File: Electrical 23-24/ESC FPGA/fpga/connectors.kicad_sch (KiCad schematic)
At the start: 2 parts, among them J3 USB_B_Micro

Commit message: Made BOM, need to modify footprints
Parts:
- added J5, J6: Conn_02x06_Top_Bottom, Connector_PinSocket_2.54mm:PinSocket_2x06_P2.54mm_Horizontal, symbol Connector_Generic:Conn_02x06_Top_Bottom
- added J7: Conn_02x20_Odd_Even, Connector_PinSocket_2.54mm:PinSocket_2x20_P2.54mm_Vertical, symbol Connector_Generic:Conn_02x20_Odd_Even
- added J8: Conn_02x06_Top_Bottom, Connector_PinSocket_2.54mm:PinSocket_2x06_P2.54mm_Vertical, symbol Connector_Generic:Conn_02x06_Top_Bottom
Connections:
- net GND: now also J5.11 (Pin_11), J5.5 (Pin_5), J6.11 (Pin_11), J6.5 (Pin_5), J7.14 (Pin_14), J7.20 (Pin_20), J7.25 (Pin_25), J7.30 (Pin_30), J7.34 (Pin_34), J7.39 (Pin_39), J7.6 (Pin_6), J7.9 (Pin_9), J8.12 (Pin_12), J8.6 (Pin_6)
- net VBATT: now also J8.1 (Pin_1), J8.7 (Pin_7)
- net VUSB: now also J7.2 (Pin_2), J7.4 (Pin_4), J8.2 (Pin_2), J8.8 (Pin_8)
- new net 1V2: J8.11 (Pin_11), J8.5 (Pin_5)
- new net 2V5: J8.10 (Pin_10), J8.4 (Pin_4)
- new net 3V3: J5.12 (Pin_12), J5.6 (Pin_6), J6.12 (Pin_12), J6.6 (Pin_6), J7.1 (Pin_1), J7.17 (Pin_17), J8.3 (Pin_3), J8.9 (Pin_9)
- new net GPIO0: J7.27 (Pin_27)
- new net GPIO1: J7.28 (Pin_28)
- new net GPIO10: J7.19 (Pin_19)
- new net GPIO11: J7.23 (Pin_23)
- new net GPIO12: J7.32 (Pin_32)
- new net GPIO13: J7.33 (Pin_33)
- new net GPIO14: J7.8 (Pin_8)
- new net GPIO15: J7.10 (Pin_10)
- new net GPIO16: J7.36 (Pin_36)
- new net GPIO17: J7.11 (Pin_11)
- new net GPIO18: J7.12 (Pin_12)
- new net GPIO19: J7.35 (Pin_35)
- new net GPIO2: J7.3 (Pin_3)
- new net GPIO20: J7.38 (Pin_38)
- new net GPIO21: J7.40 (Pin_40)
- new net GPIO22: J7.15 (Pin_15)
- new net GPIO23: J7.16 (Pin_16)
- new net GPIO24: J7.18 (Pin_18)
- new net GPIO25: J7.22 (Pin_22)
- new net GPIO26: J7.37 (Pin_37)
- new net GPIO27: J7.13 (Pin_13)
- new net GPIO3: J7.5 (Pin_5)
- new net GPIO4: J7.7 (Pin_7)
- new net GPIO5: J7.29 (Pin_29)
- new net GPIO6: J7.31 (Pin_31)
- new net GPIO7: J7.26 (Pin_26)
- new net GPIO8: J7.24 (Pin_24)
- new net GPIO9: J7.21 (Pin_21)
- new net PMOD1_0: J5.1 (Pin_1)
- new net PMOD1_1: J5.2 (Pin_2)
- new net PMOD1_2: J5.3 (Pin_3)
- new net PMOD1_3: J5.4 (Pin_4)
- new net PMOD1_4: J5.7 (Pin_7)
- new net PMOD1_5: J5.8 (Pin_8)
- new net PMOD1_6: J5.9 (Pin_9)
- new net PMOD1_7: J5.10 (Pin_10)
- new net PMOD2_0: J6.1 (Pin_1)
- new net PMOD2_1: J6.2 (Pin_2)
- new net PMOD2_2: J6.3 (Pin_3)
- new net PMOD2_3: J6.4 (Pin_4)
- new net PMOD2_4: J6.7 (Pin_7)
- new net PMOD2_5: J6.8 (Pin_8)
- new net PMOD2_6: J6.9 (Pin_9)
- new net PMOD2_7: J6.10 (Pin_10)
- no-connect marks 4 -> 5

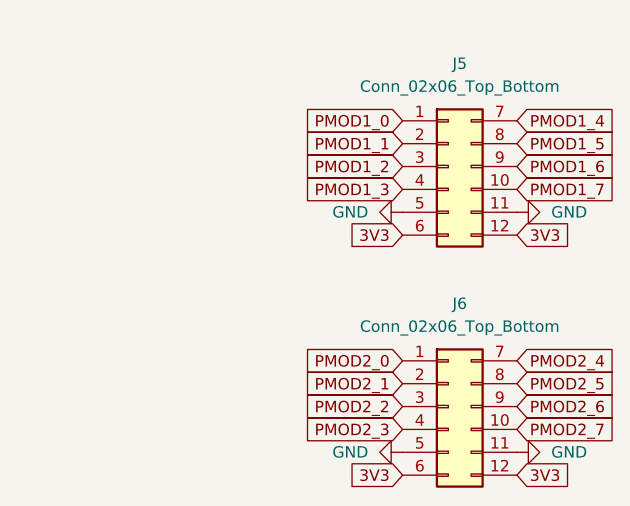
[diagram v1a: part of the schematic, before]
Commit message: Finish groupings on FPGA PCB
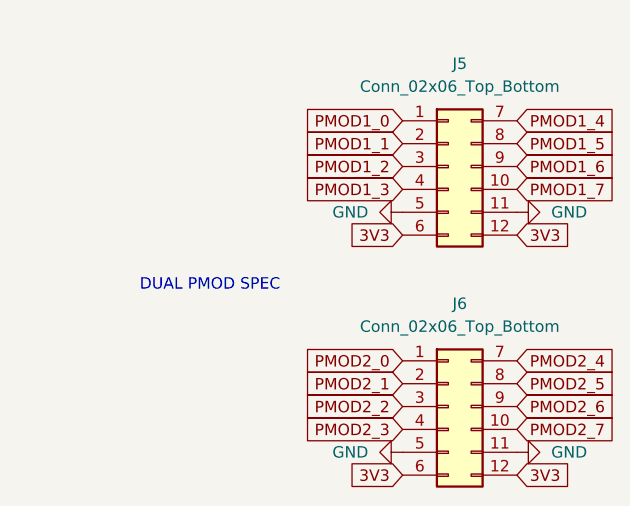
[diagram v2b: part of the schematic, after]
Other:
- note added: "DUAL PMOD SPEC"
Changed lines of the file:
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@@
   (no_connect (at 36.83 35.56))
   (no_connect (at 36.83 33.02))
+  (text "DUAL PMOD SPEC" (at 35.56 105.41 0)
+    (effects (font (size 1.27 1.27)) (justify left bottom))
+  )
   (global_label "PMOD2_1" (shape input) (at 64.77 115.57 180) (fields_autoplaced)
     (effects (font (size 1.27 1.27)) (justify right))

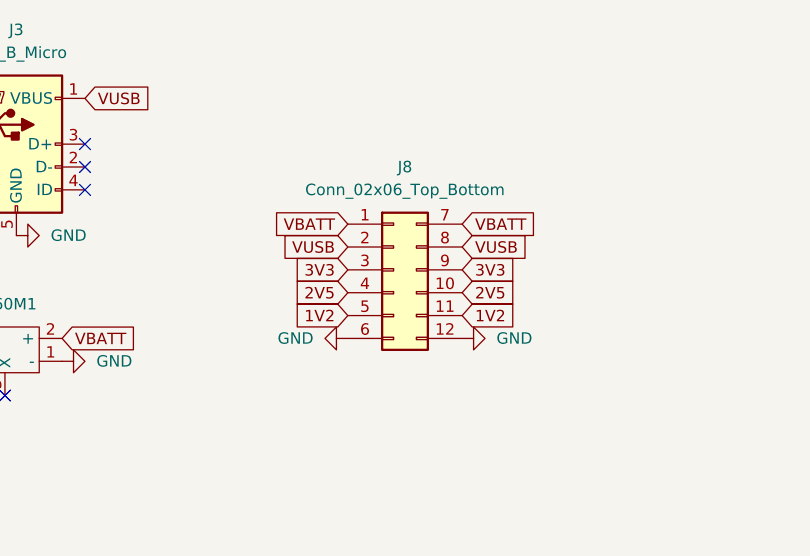
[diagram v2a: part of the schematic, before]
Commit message: Finished hard signal routing, need PMOD and Power
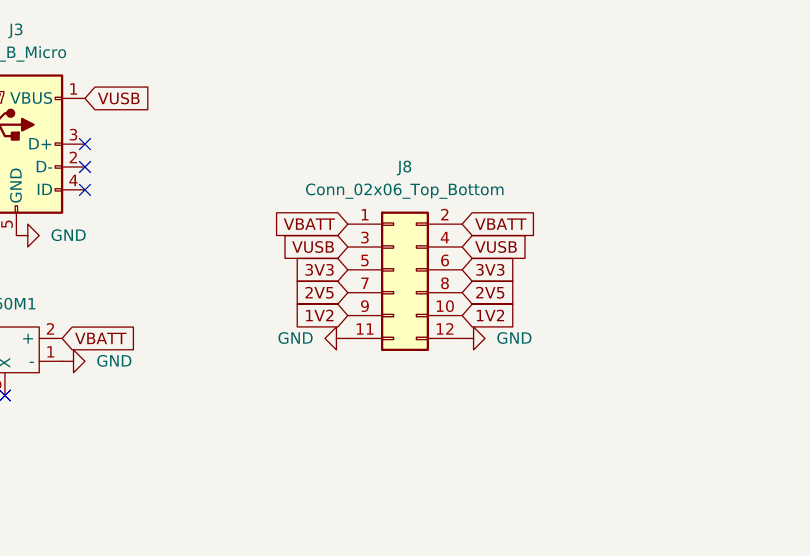
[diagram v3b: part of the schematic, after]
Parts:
- J8: symbol Connector_Generic:Conn_02x06_Top_Bottom -> Connector_Generic:Conn_02x06_Odd_Even
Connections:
- net 1V2: now also J8.10 (Pin_10), J8.9 (Pin_9); no longer J8.11 (Pin_11), J8.5 (Pin_5)
- net 2V5: now also J8.7 (Pin_7), J8.8 (Pin_8); no longer J8.10 (Pin_10), J8.4 (Pin_4)
- net 3V3: now also J8.5 (Pin_5), J8.6 (Pin_6); no longer J8.3 (Pin_3), J8.9 (Pin_9)
- net GND: now also J8.11 (Pin_11); no longer J8.6 (Pin_6)
- net VBATT: now also J8.2 (Pin_2); no longer J8.7 (Pin_7)
- net VUSB: now also J8.3 (Pin_3), J8.4 (Pin_4); no longer J8.2 (Pin_2), J8.8 (Pin_8)
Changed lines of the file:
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@@
     )
   )
-  (symbol (lib_id "Connector_Generic:Conn_02x06_Top_Bottom") (at 71.12 46.99 0) (unit 1)
+  (symbol (lib_id "Connector_Generic:Conn_02x06_Odd_Even") (at 71.12 46.99 0) (unit 1)
     (in_bom yes) (on_board yes) (dnp no) (fields_autoplaced)
     (property "Reference" "J8" (at 72.39 35.56 0)
@@
       (effects (font (size 1.27 1.27)) hide)
     )
-    (property "Datasheet" "https://www.digikey.com/en/products/detail/sullins-connector-solutions/PPTC062LFBN-RC/810212" (at 71.12 46.99 0)
+    (property "Datasheet" "~" (at 71.12 46.99 0)
       (effects (font (size 1.27 1.27)) hide)
     )

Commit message: Finish PCB layout, need to DRC
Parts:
- J5, J6: symbol Connector_Generic:Conn_02x06_Top_Bottom -> Connector_Generic:Conn_02x06_Odd_Even
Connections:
- net 3V3: now also J5.11 (Pin_11), J6.11 (Pin_11); no longer J5.6 (Pin_6), J6.6 (Pin_6)
- net GND: now also J5.10 (Pin_10), J5.9 (Pin_9), J6.10 (Pin_10), J6.9 (Pin_9); no longer J5.11 (Pin_11), J5.5 (Pin_5), J6.11 (Pin_11), J6.5 (Pin_5)
- net PMOD1_1: now also J5.3 (Pin_3); no longer J5.2 (Pin_2)
- net PMOD1_2: now also J5.5 (Pin_5); no longer J5.3 (Pin_3)
- net PMOD1_3: now also J5.7 (Pin_7); no longer J5.4 (Pin_4)
- net PMOD1_4: now also J5.2 (Pin_2); no longer J5.7 (Pin_7)
- net PMOD1_5: now also J5.4 (Pin_4); no longer J5.8 (Pin_8)
- net PMOD1_6: now also J5.6 (Pin_6); no longer J5.9 (Pin_9)
- net PMOD1_7: now also J5.8 (Pin_8); no longer J5.10 (Pin_10)
- net PMOD2_1: now also J6.3 (Pin_3); no longer J6.2 (Pin_2)
- net PMOD2_2: now also J6.5 (Pin_5); no longer J6.3 (Pin_3)
- net PMOD2_3: now also J6.7 (Pin_7); no longer J6.4 (Pin_4)
- net PMOD2_4: now also J6.2 (Pin_2); no longer J6.7 (Pin_7)
- net PMOD2_5: now also J6.4 (Pin_4); no longer J6.8 (Pin_8)
- net PMOD2_6: now also J6.6 (Pin_6); no longer J6.9 (Pin_9)
- net PMOD2_7: now also J6.8 (Pin_8); no longer J6.10 (Pin_10)
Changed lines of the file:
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@@
     )
   )
-  (symbol (lib_id "Connector_Generic:Conn_02x06_Top_Bottom") (at 69.85 118.11 0) (unit 1)
+  (symbol (lib_id "Connector_Generic:Conn_02x06_Odd_Even") (at 69.85 118.11 0) (unit 1)
     (in_bom yes) (on_board yes) (dnp no) (fields_autoplaced)
     (property "Reference" "J6" (at 71.12 106.68 0)
@@
       (effects (font (size 1.27 1.27)) hide)
     )
-    (property "Datasheet" "https://www.digikey.com/en/products/detail/sullins-connector-solutions/PPTC062LJBN-RC/775978" (at 69.85 118.11 0)
+    (property "Datasheet" "~" (at 69.85 118.11 0)
       (effects (font (size 1.27 1.27)) hide)
     )
@@
     )
   )
-  (symbol (lib_id "Connector_Generic:Conn_02x06_Top_Bottom") (at 69.85 91.44 0) (unit 1)
+  (symbol (lib_id "Connector_Generic:Conn_02x06_Odd_Even") (at 69.85 91.44 0) (unit 1)
     (in_bom yes) (on_board yes) (dnp no) (fields_autoplaced)
     (property "Reference" "J5" (at 71.12 80.01 0)
@@
       (effects (font (size 1.27 1.27)) hide)
     )
-    (property "Datasheet" "https://www.digikey.com/en/products/detail/sullins-connector-solutions/PPTC062LJBN-RC/775978" (at 69.85 91.44 0)
-      (effects (font (size 1.27 1.27)) hide)
-    )
+    (property "Datasheet" "~" (at 69.85 91.44 0)
+      (effects (font (size 1.27 1.27)) hide)
+    )

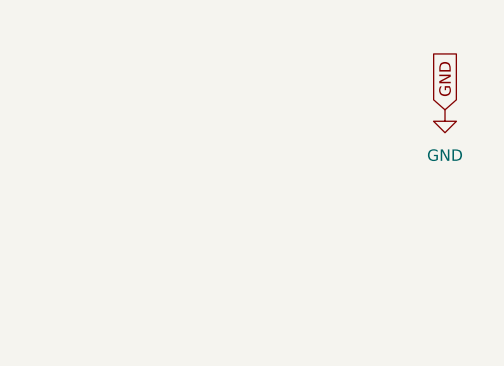
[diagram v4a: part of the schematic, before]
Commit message: Turn XT60
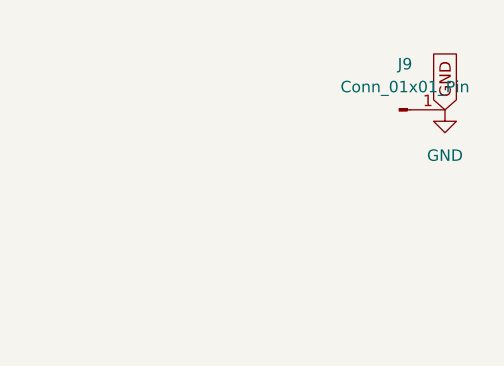
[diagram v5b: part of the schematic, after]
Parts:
- added J9: Conn_01x01_Pin, fpga:RASPI, symbol Connector:Conn_01x01_Pin
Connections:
- net GND: now also J9.1 (Pin_1)
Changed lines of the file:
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@@
+    )
+  )
+  (symbol (lib_id "Connector:Conn_01x01_Pin") (at 267.97 29.21 0) (unit 1)
+    (in_bom yes) (on_board yes) (dnp no) (fields_autoplaced)
+    (property "Reference" "J9" (at 268.605 24.13 0)
+      (effects (font (size 1.27 1.27)))
+    )
+    (property "Value" "Conn_01x01_Pin" (at 268.605 26.67 0)
+      (effects (font (size 1.27 1.27)))
+    )
+    (property "Footprint" "fpga:RASPI" (at 267.97 29.21 0)
+      (effects (font (size 1.27 1.27)) hide)
+    )
+    (property "Datasheet" "~" (at 267.97 29.21 0)
+      (effects (font (size 1.27 1.27)) hide)
+    )
+    (pin "1")
+    (instances
+      (project "fpga"
+        (path "/5bf59577-a814-4364-8f7a-37815cfb5474/7f7a1c48-365b-4a0e-b4b9-fce51f39bb27"
+          (reference "J9") (unit 1)
+        )
+      )
     )
   )
